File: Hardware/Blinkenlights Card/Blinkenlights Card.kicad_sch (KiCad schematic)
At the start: 73 parts, among them J1 6502CARDEDGE

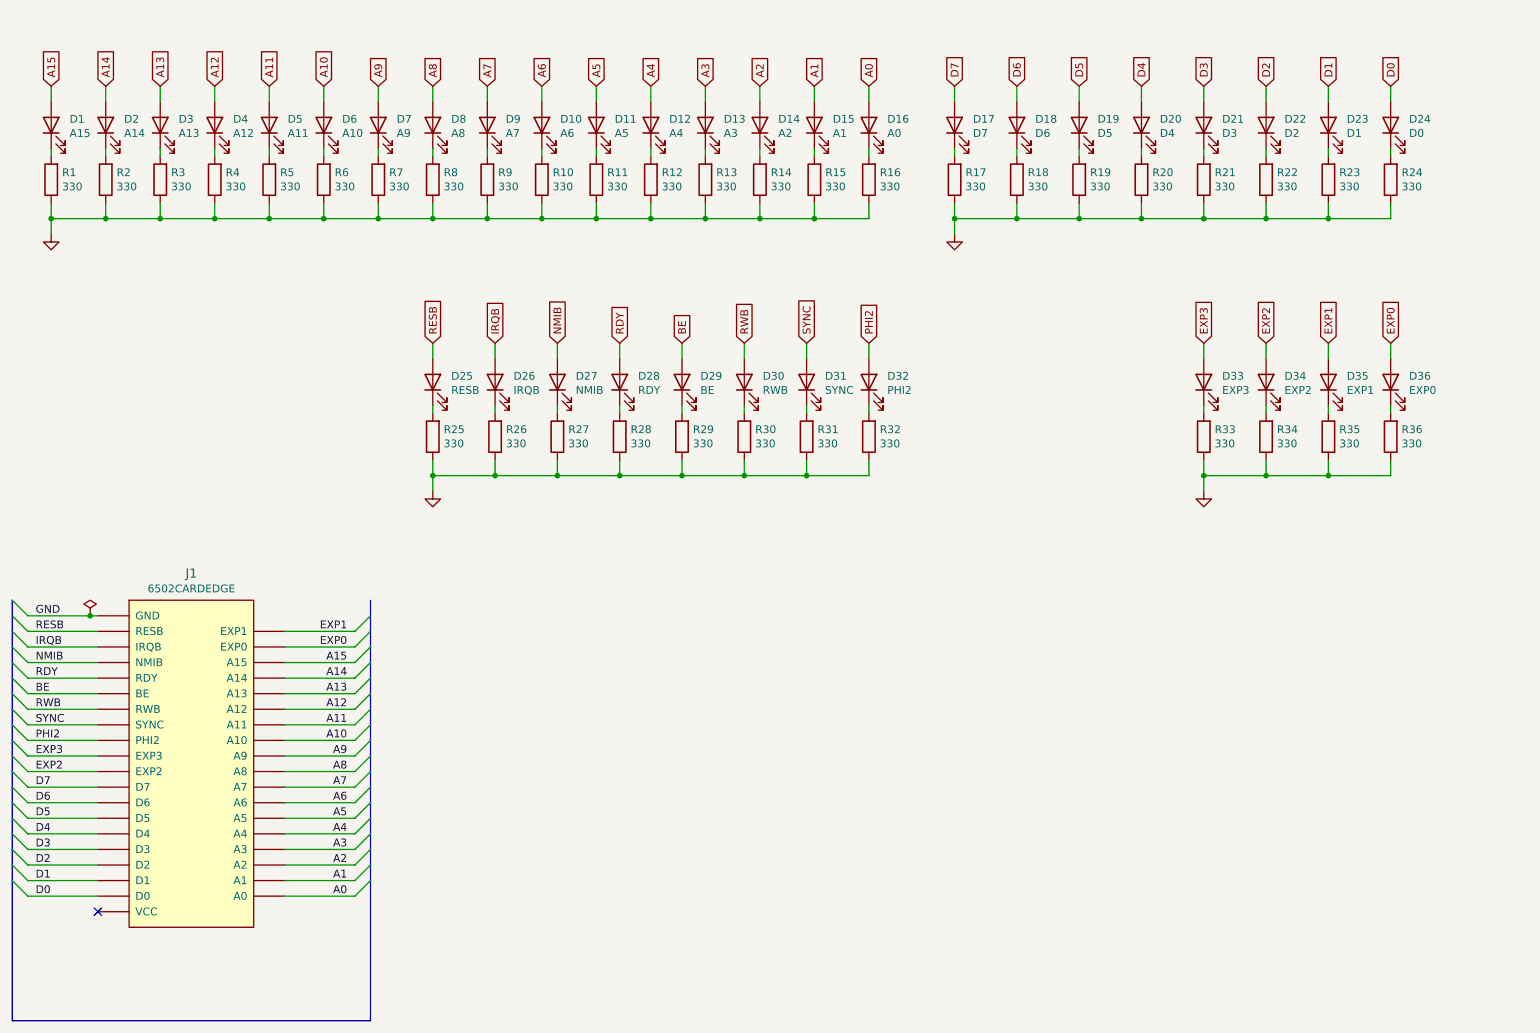
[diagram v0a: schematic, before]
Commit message: Proper debugger logging
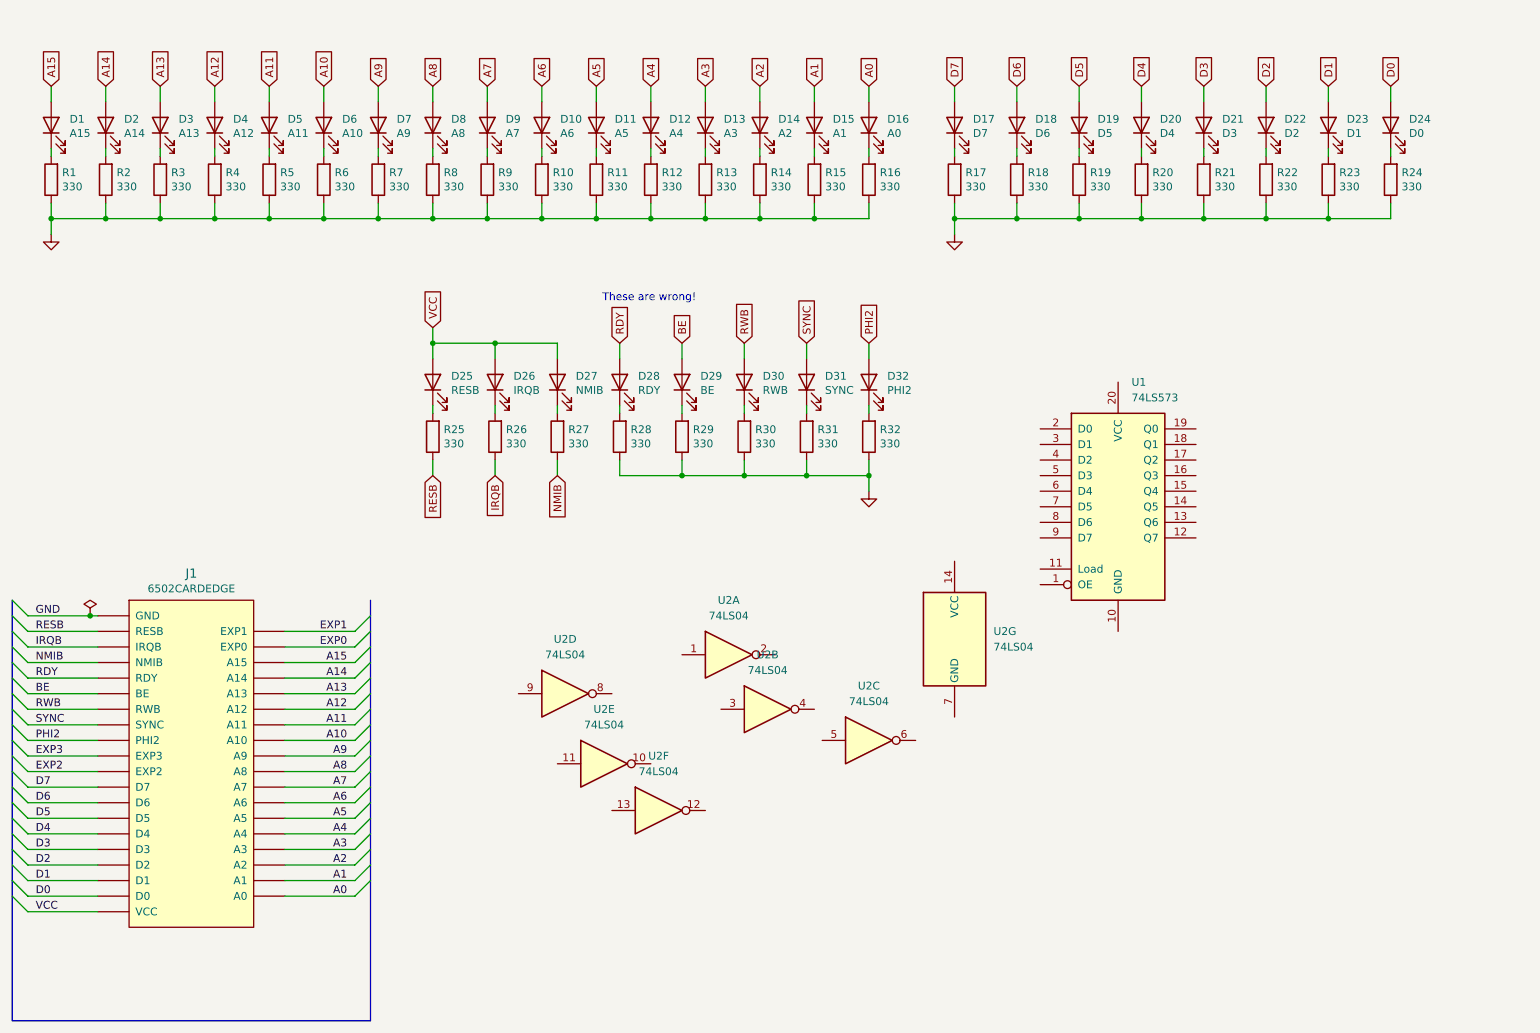
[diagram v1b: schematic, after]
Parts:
- removed D33: EXP3, LED_SMD:LED_0805_2012Metric, symbol Device:LED
- removed D34: EXP2, LED_SMD:LED_0805_2012Metric, symbol Device:LED
- removed D35: EXP1, LED_SMD:LED_0805_2012Metric, symbol Device:LED
- removed D36: EXP0, LED_SMD:LED_0805_2012Metric, symbol Device:LED
- removed R33, R34, R35, R36: 330, Resistor_SMD:R_0805_2012Metric, symbol Device:R
- added U1: 74LS573, symbol 74xx:74LS573
- added U2: 74LS04, symbol 74xx:74LS04
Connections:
- net GND: no longer R25.1, R26.1, R27.1
- net IRQB: now also R26.1; no longer D26.2 (A)
- net NMIB: now also R27.1; no longer D27.2 (A)
- net RESB: now also R25.1; no longer D25.2 (A)
- net VCC: now also D25.2 (A), D26.2 (A), D27.2 (A)
- no-connect marks 1 -> 0
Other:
- note added: "These are wrong!"

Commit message: Reworking some schematics
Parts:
- added U1, U4: 74LS573, Package_SO:SOP-20_7.5x12.8mm_P1.27mm, symbol 74xx:74LS573
- U2: renamed from U1; footprint (none) -> Package_SO:SOP-20_7.5x12.8mm_P1.27mm; LCSC (none) -> C6851434
- U3: renamed from U2; footprint (none) -> Package_SO:SOIC-14_3.9x8.7mm_P1.27mm; LCSC (none) -> C86613
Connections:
- net A0: now also U1.2 (D0); no longer D16.2 (A)
- net A1: now also U1.3 (D1); no longer D15.2 (A)
- net A10: now also U2.4 (D2); no longer D6.2 (A)
- net A11: now also U2.5 (D3); no longer D5.2 (A)
- net A12: now also U2.6 (D4); no longer D4.2 (A)
- net A13: now also U2.7 (D5); no longer D3.2 (A)
- net A14: now also U2.8 (D6); no longer D2.2 (A)
- net A15: now also U2.9 (D7); no longer D1.2 (A)
- net A2: now also U1.4 (D2); no longer D14.2 (A)
- net A3: now also U1.5 (D3); no longer D13.2 (A)
- net A4: now also U1.6 (D4); no longer D12.2 (A)
- net A5: now also U1.7 (D5); no longer D11.2 (A)
- net A6: now also U1.8 (D6); no longer D10.2 (A)
- net A7: now also U1.9 (D7); no longer D9.2 (A)
- net A8: now also U2.2 (D0); no longer D8.2 (A)
- net A9: now also U2.3 (D1); no longer D7.2 (A)
- net BE: now also U3.9; no longer D29.2 (A)
- net D0: now also U4.2 (D0); no longer D24.2 (A)
- net D1: now also U4.3 (D1); no longer D23.2 (A)
- net D2: now also U4.4 (D2); no longer D22.2 (A)
- net D3: now also U4.5 (D3); no longer D21.2 (A)
- net D4: now also U4.6 (D4); no longer D20.2 (A)
- net D5: now also U4.7 (D5); no longer D19.2 (A)
- net D6: now also U4.8 (D6); no longer D18.2 (A)
- net D7: now also U4.9 (D7); no longer D17.2 (A)
- net GND: now also U2.1 (OE), U2.10 (GND), U3.5, U3.7 (GND), U1.1 (OE), U1.10 (GND), U4.1 (OE), U4.10 (GND)
- net PHI2: now also U2.11 (Load), U3.13, U1.11 (Load)
- net RDY: now also U3.1; no longer D28.2 (A)
- net VCC: now also U2.20 (VCC), U3.14 (VCC), U1.20 (VCC), U4.20 (VCC)
- net at U3.8: now also U3.11
- net at U3.3: now also U3.2
- net RDY_LED: now reaches U3.4
- net RDY_LED: now also D28.2 (A)
- net at U3.12: now also U4.11 (Load)
- net BE_LED: now reaches U3.10
- net BE_LED: now also D29.2 (A)
- net A15_LED: now reaches U2.12 (Q7)
- net A15_LED: now also D1.2 (A)
- net A14_LED: now reaches U2.13 (Q6)
- net A14_LED: now also D2.2 (A)
- net A13_LED: now reaches U2.14 (Q5)
- net A13_LED: now also D3.2 (A)
- net A12_LED: now reaches U2.15 (Q4)
- net A12_LED: now also D4.2 (A)
- net A11_LED: now reaches U2.16 (Q3)
- net A11_LED: now also D5.2 (A)
- net A10_LED: now reaches U2.17 (Q2)
- net A10_LED: now also D6.2 (A)
- net A9_LED: now reaches U2.18 (Q1)
- net A9_LED: now also D7.2 (A)
- net A8_LED: now reaches U2.19 (Q0)
- net A8_LED: now also D8.2 (A)
- net EXP0: no longer names the net of J1.EXP0
- net EXP1: no longer names the net of J1.EXP1
- net EXP2: no longer names the net of J1.EXP2
- net EXP3: no longer names the net of J1.EXP3
- new net A0_LED: D16.2 (A), U1.19 (Q0)
- new net A1_LED: D15.2 (A), U1.18 (Q1)
- new net A2_LED: D14.2 (A), U1.17 (Q2)
- new net A3_LED: D13.2 (A), U1.16 (Q3)
- new net A4_LED: D12.2 (A), U1.15 (Q4)
- new net A5_LED: D11.2 (A), U1.14 (Q5)
- new net A6_LED: D10.2 (A), U1.13 (Q6)
- new net A7_LED: D9.2 (A), U1.12 (Q7)
- new net D0_LED: D24.2 (A), U4.19 (Q0)
- new net D1_LED: D23.2 (A), U4.18 (Q1)
- new net D2_LED: D22.2 (A), U4.17 (Q2)
- new net D3_LED: D21.2 (A), U4.16 (Q3)
- new net D4_LED: D20.2 (A), U4.15 (Q4)
- new net D5_LED: D19.2 (A), U4.14 (Q5)
- new net D6_LED: D18.2 (A), U4.13 (Q6)
- new net D7_LED: D17.2 (A), U4.12 (Q7)
- no-connect marks 0 -> 5
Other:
- note removed: "These are wrong!"
- moved on the sheet: D25, D26, D27, D28, D29, D30, D31, D32, R25, R26, R27, R28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

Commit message: Add GPIO cards
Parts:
- U1, U2, U4: value 74LS573 -> 74HC573; footprint Package_SO:SOP-20_7.5x12.8mm_P1.27mm -> Package_SO:SOIC-20W_7.5x12.8mm_P1.27mm; LCSC C6851434 -> C5608
- U3: value 74LS04 -> 74HC04; LCSC C86613 -> C5590
- U3: value 74LS04 -> 74HC04; symbol 74xx:74LS04 -> 74xx:74HC04; LCSC C86613 -> C5590
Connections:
- net GND: no longer U3.5
- net at U3.6: now also U4.11 (Load)
- net at U3.12: now also U3.5; no longer U4.11 (Load)
- no-connect marks 5 -> 4
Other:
- moved on the sheet: U3C, U3F, U3G

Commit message: Cleanup
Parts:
- J1: value 6502CARDEDGE -> 6502 Card Edge; footprint 6502 Parts:6502CARDEDGE -> 6502 Parts:6502 Card Edge; symbol 6502 Parts:6502CARDEDGE -> 6502 Parts:6502 Card Edge

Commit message: Cleanup
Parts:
- added C1, C2, C3, C4: 100nF, Capacitor_SMD:C_0805_2012Metric, symbol Device:C
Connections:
- net GND: now also C1.2, C2.2, C3.2, C4.2
- net VCC: now also C1.1, C2.1, C3.1, C4.1
